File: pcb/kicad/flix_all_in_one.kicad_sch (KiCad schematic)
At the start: 0 parts

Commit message: Updated sch and added BoM.md
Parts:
- added U1: ESP32-WROOM-32E, RF_Module:ESP32-WROOM-32E, symbol RF_Module:ESP32-WROOM-32E
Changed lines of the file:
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@@
 	(generator_version "10.0")
 	(paper "A4")
+	(symbol
+		(lib_id "RF_Module:ESP32-WROOM-32E")
+		(at 148.59 102.87 0)
+		(unit 1)
+		(body_style 1)
+		(exclude_from_sim no)
+		(in_bom yes)
+		(on_board yes)
+		(in_pos_files yes)
+		(dnp no)
+		(fields_autoplaced yes)
+		(property "Reference" "U1"
+			(at 150.7333 64.77 0)
+			(show_name no)
+			(do_not_autoplace no)
+			(effects
+				(font
+					(size 1.27 1.27)
+				)
+				(justify left)
+			)
+		)
+		(property "Value" "ESP32-WROOM-32E"
+			(at 150.7333 67.31 0)
+			(show_name no)
+			(do_not_autoplace no)
+			(effects
+				(font
+					(size 1.27 1.27)
+				)
+				(justify left)
+			)
+		)
+		(property "Footprint" "RF_Module:ESP32-WROOM-32E"
+			(at 165.1 137.16 0)
+			(hide yes)
+			(show_name no)
+			(do_not_autoplace no)
+			(effects
+				(font
+					(size 1.27 1.27)
+				)
+			)
+		)
+		(property "Datasheet" "https://www.espressif.com/sites/default/files/documentation/esp32-wroom-32e_esp32-wroom-32ue_datasheet_en.pdf"
+			(at 148.59 102.87 0)
+			(hide yes)
+			(show_name no)
+			(do_not_autoplace no)
+			(effects
+				(font
+					(size 1.27 1.27)
+				)
+			)
+		)
+		(property "Description" "RF Module, ESP32-D0WD-V3 SoC, without PSRAM, Wi-Fi 802.11b/g/n, Bluetooth, BLE, 32-bit, 2.7-3.6V, onboard antenna, SMD"
+			(at 148.59 102.87 0)
+			(hide yes)
+			(show_name no)
+			(do_not_autoplace no)
+			(effects
+				(font
+					(size 1.27 1.27)
+				)
+			)
+		)
+		(pin "14"
+		)
+		(pin "11"
+		)
+		(pin "16"
+		)
+		(pin "12"
+		)
+		(pin "9"
+		)
+		(pin "17"
+		)
+		(pin "13"
+		)
+		(pin "30"
+		)
+		(pin "33"
+		)
+		(pin "27"
+		)
+		(pin "31"
+		)
+		(pin "10"
+		)
+		(pin "32"
+		)
+		(pin "34"
+		)
+		(pin "18"
+		)
+		(pin "26"
+		)
+		(pin "28"
+		)
+		(pin "19"
+		)
+		(pin "21"
+		)
+		(pin "35"
+		)
+		(pin "36"
+		)
+		(pin "29"
+		)
+		(pin "[1,15,38,39]"
+		)
+		(pin "3"
+		)
+		(pin "2"
+		)
+		(pin "20"
+		)
+		(pin "4"
+		)
+		(pin "25"
+		)
+		(pin "6"
+		)
+		(pin "24"
+		)
+		(pin "5"
+		)
+		(pin "7"
+		)
+		(pin "8"
+		)
+		(pin "37"
+		)
+		(pin "22"
+		)
+		(pin "23"
+		)
+		(instances
+			(project "flix_all_in_one"
+				(path "/b72e5080-03e0-4f53-a508-ed803e54cf11"
+					(reference "U1")
+					(unit 1)
+				)
+			)
+		)
+	)
 	(sheet_instances
 		(path "/"

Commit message: .
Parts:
- removed U1: ESP32-WROOM-32E, RF_Module:ESP32-WROOM-32E, symbol RF_Module:ESP32-WROOM-32E
- added U1: ESP32-WROOM-E, PCM_Espressif:ESP32-WROOM-32E, symbol PCM_Espressif:ESP32-WROOM-E
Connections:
- new net: U1.1 (GND), U1.15 (GND), U1.38 (GND)
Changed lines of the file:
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@@
 	(paper "A4")
 	(symbol
-		(lib_id "RF_Module:ESP32-WROOM-32E")
-		(at 148.59 102.87 0)
+		(lib_id "PCM_Espressif:ESP32-WROOM-E")
+		(at 195.58 68.58 0)
 		(unit 1)
 		(body_style 1)
@@
 		(fields_autoplaced yes)
 		(property "Reference" "U1"
-			(at 150.7333 64.77 0)
+			(at 197.7233 40.64 0)
 			(show_name no)
 			(do_not_autoplace no)
@@
 			)
 		)
-		(property "Value" "ESP32-WROOM-32E"
-			(at 150.7333 67.31 0)
+		(property "Value" "ESP32-WROOM-E"
+			(at 197.7233 43.18 0)
 			(show_name no)
 			(do_not_autoplace no)
@@
 			)
 		)
-		(property "Footprint" "RF_Module:ESP32-WROOM-32E"
-			(at 165.1 137.16 0)
+		(property "Footprint" "PCM_Espressif:ESP32-WROOM-32E"
+			(at 195.58 104.14 0)
 			(hide yes)
 			(show_name no)
@@
 		)
 		(property "Datasheet" "https://www.espressif.com/sites/default/files/documentation/esp32-wroom-32e_esp32-wroom-32ue_datasheet_en.pdf"
-			(at 148.59 102.87 0)
+			(at 195.58 106.68 0)
 			(hide yes)
 			(show_name no)
@@
 			)
 		)
-		(property "Description" "RF Module, ESP32-D0WD-V3 SoC, without PSRAM, Wi-Fi 802.11b/g/n, Bluetooth, BLE, 32-bit, 2.7-3.6V, onboard antenna, SMD"
-			(at 148.59 102.87 0)
+		(property "Description" "ESP32-WROOM-32E integrates ESP32-D0WD-V3, with higher stability and safety performance."
+			(at 195.58 68.58 0)
 			(hide yes)
 			(show_name no)
@@
 			)
 		)
-		(pin "14"
+		(pin "15"
 		)
-		(pin "11"
+		(pin "30"
 		)
-		(pin "16"
-		)
-		(pin "12"
-		)
-		(pin "9"
-		)
-		(pin "17"
+		(pin "31"
 		)
 		(pin "13"
 		)
-		(pin "30"
-		)
-		(pin "33"
-		)
-		(pin "27"
-		)
-		(pin "31"
-		)
-		(pin "10"
-		)
-		(pin "32"
-		)
-		(pin "34"
-		)
-		(pin "18"
-		)
-		(pin "26"
-		)
-		(pin "28"
-		)
-		(pin "19"
-		)
-		(pin "21"
+		(pin "25"
 		)
 		(pin "35"
@@
 		(pin "36"
 		)
+		(pin "33"
+		)
 		(pin "29"
 		)
-		(pin "[1,15,38,39]"
+		(pin "34"
+		)
+		(pin "37"
+		)
+		(pin "14"
+		)
+		(pin "7"
+		)
+		(pin "26"
+		)
+		(pin "9"
+		)
+		(pin "27"
+		)
+		(pin "5"
+		)
+		(pin "4"
 		)
 		(pin "3"
 		)
-		(pin "2"
+		(pin "23"
 		)
-		(pin "20"
+		(pin "39"
 		)
-		(pin "4"
+		(pin "12"
 		)
-		(pin "25"
+		(pin "28"
+		)
+		(pin "16"
+		)
+		(pin "38"
+		)
+		(pin "11"
+		)
+		(pin "8"
+		)
+		(pin "10"
 		)
 		(pin "6"
 		)
+		(pin "2"
+		)
+		(pin "1"
+		)
 		(pin "24"
 		)
-		(pin "5"
-		)
-		(pin "7"
-		)
-		(pin "8"
-		)
-		(pin "37"
-		)
-		(pin "22"
-		)
-		(pin "23"
-		)
 		(instances

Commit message: updated sch
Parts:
- added IC1: CP2102C-A01-GQFN28, QFN50P500X500X80-29N-D, symbol CP2102C-A01-GQFN28:CP2102C-A01-GQFN28
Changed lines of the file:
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@@
 	(paper "A4")
+	(symbol
+		(lib_id "CP2102C-A01-GQFN28:CP2102C-A01-GQFN28")
+		(at 45.72 48.26 0)
+		(unit 1)
+		(body_style 1)
+		(exclude_from_sim no)
+		(in_bom yes)
+		(on_board yes)
+		(in_pos_files yes)
+		(dnp no)
+		(fields_autoplaced yes)
+		(property "Reference" "IC1"
+			(at 86.36 41.8398 0)
+			(show_name no)
+			(do_not_autoplace no)
+			(effects
+				(font
+					(size 1.27 1.27)
+				)
+			)
+		)
+		(property "Value" "CP2102C-A01-GQFN28"
+			(at 86.36 44.3798 0)
+			(show_name no)
+			(do_not_autoplace no)
+			(effects
+				(font
+					(size 1.27 1.27)
+				)
+			)
+		)
+		(property "Footprint" "QFN50P500X500X80-29N-D"
+			(at 74.93 133.02 0)
+			(hide yes)
+			(show_name no)
+			(do_not_autoplace no)
+			(effects
+				(font
+					(size 1.27 1.27)
+				)
+				(justify left top)
+			)
+		)
+		(property "Datasheet" "https://www.silabs.com/documents/public/data-sheets/cp2102c-datasheet.pdf"
+			(at 74.93 233.02 0)
+			(hide yes)
+			(show_name no)
+			(do_not_autoplace no)
+			(effects
+				(font
+					(size 1.27 1.27)
+				)
+				(justify left top)
+			)
+		)
+		(property "Description" "USB Interface IC Single Chip - USB to UART Bridge QFN28 -40 to +85 C"
+			(at 45.72 48.26 0)
+			(hide yes)
+			(show_name no)
+			(do_not_autoplace no)
+			(effects
+				(font
+					(size 1.27 1.27)
+				)
+			)
+		)
+		(property "Height" "0.8"
+			(at 74.93 433.02 0)
+			(hide yes)
+			(show_name no)
+			(do_not_autoplace no)
+			(effects
+				(font
+					(size 1.27 1.27)
+				)
+				(justify left top)
+			)
+		)
+		(property "Mouser Part Number" "634-P2102CA01GQFN28"
+			(at 74.93 533.02 0)
+			(hide yes)
+			(show_name no)
+			(do_not_autoplace no)
+			(effects
+				(font
+					(size 1.27 1.27)
+				)
+				(justify left top)
+			)
+		)
+		(property "Mouser Price/Stock" "https://www.mouser.co.uk/ProductDetail/Silicon-Labs/CP2102C-A01-GQFN28?qs=NeOn4crkEus2KwttjYlKhg%3D%3D"
+			(at 74.93 633.02 0)
+			(hide yes)
+			(show_name no)
+			(do_not_autoplace no)
+			(effects
+				(font
+					(size 1.27 1.27)
+				)
+				(justify left top)
+			)
+		)
+		(property "Manufacturer_Name" "Silicon Labs"
+			(at 74.93 733.02 0)
+			(hide yes)
+			(show_name no)
+			(do_not_autoplace no)
+			(effects
+				(font
+					(size 1.27 1.27)
+				)
+				(justify left top)
+			)
+		)
+		(property "Manufacturer_Part_Number" "CP2102C-A01-GQFN28"
+			(at 74.93 833.02 0)
+			(hide yes)
+			(show_name no)
+			(do_not_autoplace no)
+			(effects
+				(font
+					(size 1.27 1.27)
+				)
+				(justify left top)
+			)
+		)
+		(pin "10"
+		)
+		(pin "12"
+		)
+		(pin "14"
+		)
+		(pin "13"
+		)
+		(pin "11"
+		)
+		(pin "15"
+		)
+		(pin "9"
+		)
+		(pin "3"
+		)
+		(pin "6"
+		)
+		(pin "7"
+		)
+		(pin "2"
+		)
+		(pin "5"
+		)
+		(pin "4"
+		)
+		(pin "19"
+		)
+		(pin "1"
+		)
+		(pin "17"
+		)
+		(pin "28"
+		)
+		(pin "20"
+		)
+		(pin "21"
+		)
+		(pin "18"
+		)
+		(pin "8"
+		)
+		(pin "29"
+		)
+		(pin "22"
+		)
+		(pin "23"
+		)
+		(pin "24"
+		)
+		(pin "16"
+		)
+		(pin "25"
+		)
+		(pin "26"
+		)
+		(pin "27"
+		)
+		(instances
+			(project "flix_all_in_one"
+				(path "/b72e5080-03e0-4f53-a508-ed803e54cf11"
+					(reference "IC1")
+					(unit 1)
+				)
+			)
+		)
+	)
 	(symbol
 		(lib_id "PCM_Espressif:ESP32-WROOM-E")

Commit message: updated BoM, Libs and SCH
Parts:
- added D1, D2, D3: SLESD5LM5.0CS, SODFL1608X70N, symbol SLESD5LM5.0CS:SLESD5LM5.0CS
- added IC2: BMP384, BMP384, symbol BMP384:BMP384
- added J1: UJ20-C-H-G-MSMT-2B-P16-TR, UJ20-C-H-G-MSMT-2B-P16-TR:SAMESKY_UJ20-C-H-G-MSMT-2B-P16-TR, symbol UJ20-C-H-G-MSMT-2B-P16-TR:UJ20-C-H-G-MSMT-2B-P16-TR
- added J2: BM03B-GHS-TBT_LF__SN__N_, BM03B-GHS-TBT_LF__SN__N_:CONN_BM03B-GHS-TBT_LF__SN__N_, symbol BM03B-GHS-TBT_LF__SN__N_:BM03B-GHS-TBT_LF__SN__N_
- added J3, J4, J5: BM02B-GHS-TBT_LF__SN__N_, BM02B-GHS-TBT_LF__SN__N_:JST_BM02B-GHS-TBT_LF__SN__N_, symbol BM02B-GHS-TBT_LF__SN__N_:BM02B-GHS-TBT_LF__SN__N_
- added S1: TS21-34-035-BK-260-SMT-TR, TS21-34-035-BK-260-SMT-TR:SW_TS21-34-035-BK-260-SMT-TR, symbol TS21-34-035-BK-260-SMT-TR:TS21-34-035-BK-260-SMT-TR
- added U2: ICM-40609-D, ICM-40609-D:XDCR_ICM-40609-D, symbol ICM-40609-D:ICM-40609-D
- added U3: TP4054ST25P, C382138:SOT-23-5_L2.9-W1.6-P0.95-LS2.8-BL, symbol TP4054ST25P:TP4054ST25P
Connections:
- new net: J1.SH1 (SHIELD), J1.SH2 (SHIELD), J1.SH3 (SHIELD), J1.SH4 (SHIELD)
- new net: U2.1 (NC), U2.10 (NC), U2.14 (NC), U2.15 (NC), U2.16 (NC), U2.17 (NC), U2.2 (NC), U2.21 (NC), U2.3 (NC), U2.4 (NC), U2.5 (NC), U2.6 (NC), U2.7 (NC)
- new net: U2.11 (RESV), U2.20 (RESV)
- new net: J5.S1 (SHIELD), J5.S2 (SHIELD)
- new net: J4.S1 (SHIELD), J4.S2 (SHIELD)
- new net: J3.S1 (SHIELD), J3.S2 (SHIELD)
- new net: J2.4 (SHIELD), J2.5 (SHIELD)
- new net GND: J1.A1/B12 (GND), J1.B1/A12 (GND)
- new net VBUS: J1.A4/B9 (VBUS), J1.B4/A9 (VBUS)

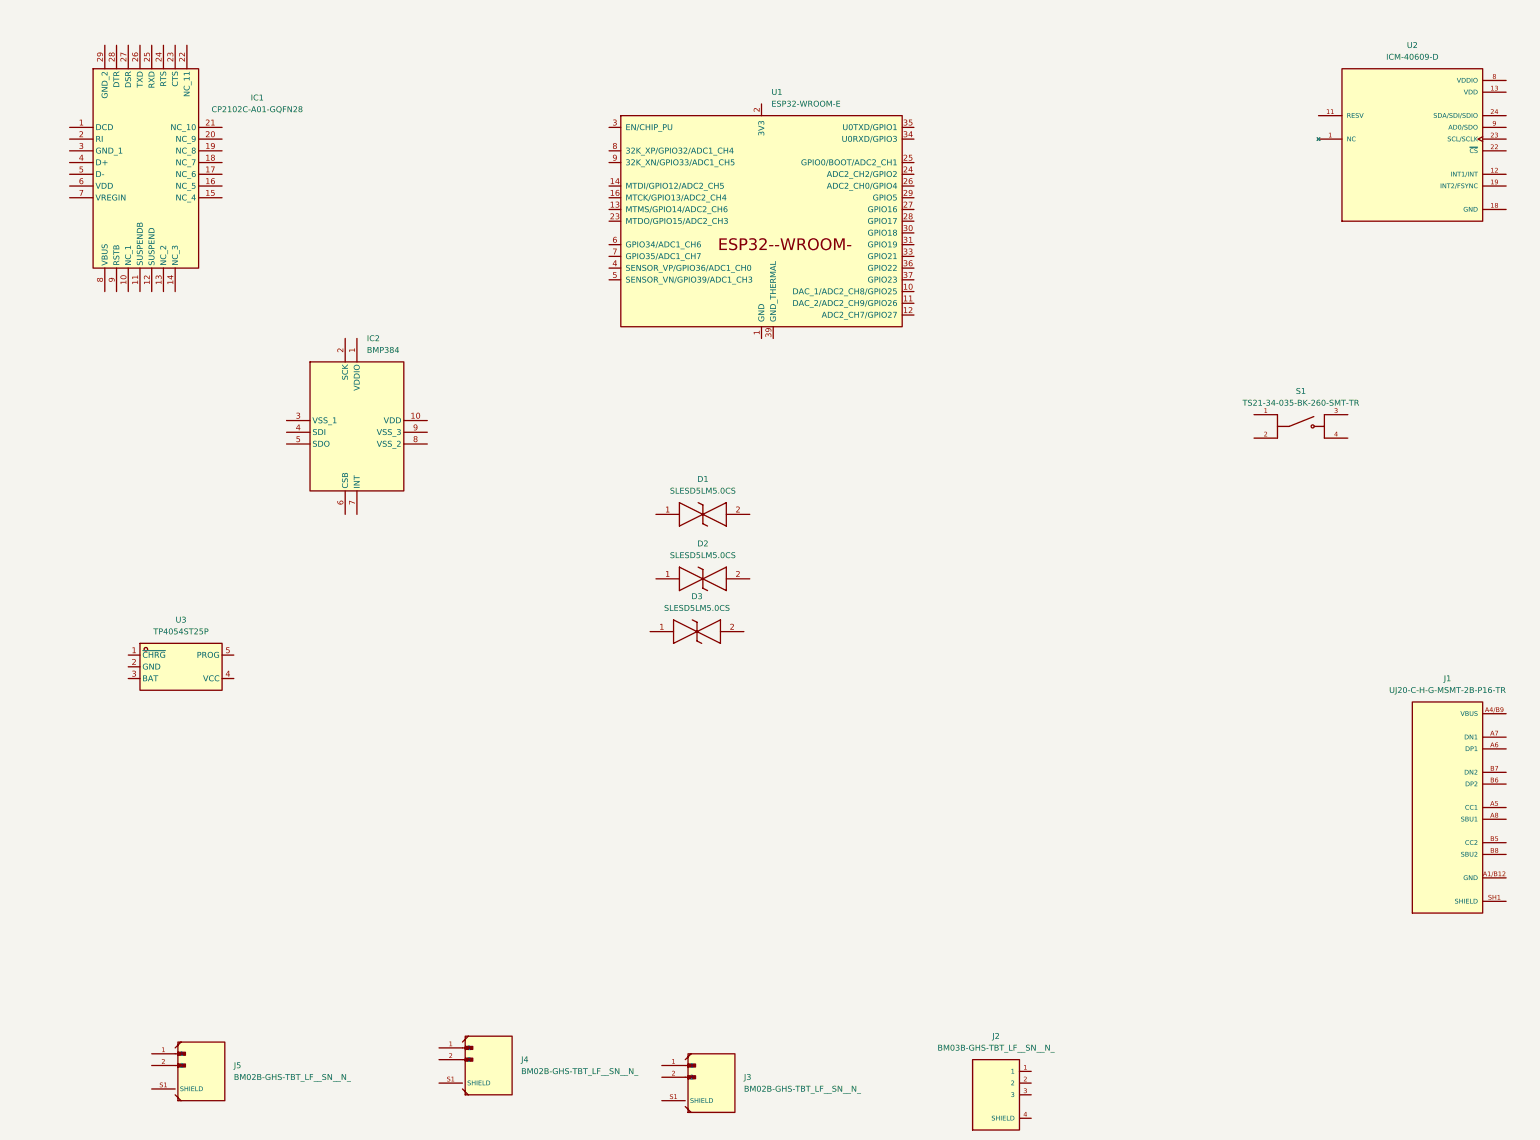
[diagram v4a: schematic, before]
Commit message: update lib and sch
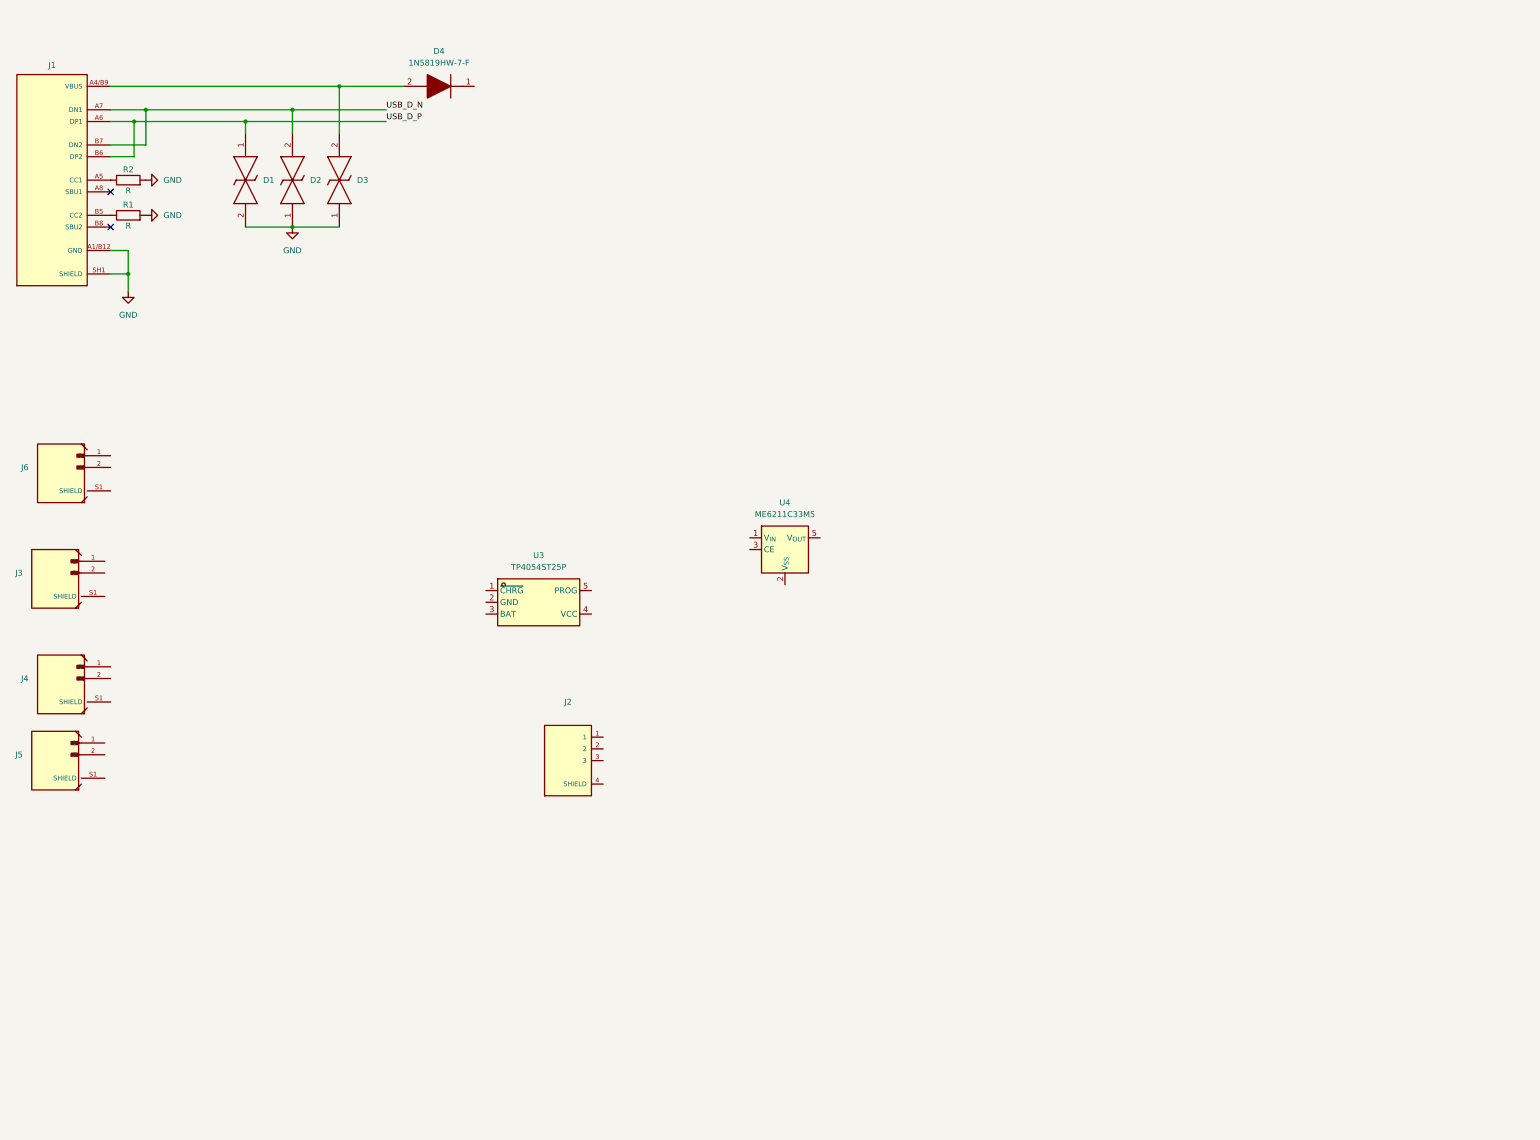
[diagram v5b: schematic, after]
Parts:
- removed IC1: CP2102C-A01-GQFN28, QFN50P500X500X80-29N-D, symbol CP2102C-A01-GQFN28:CP2102C-A01-GQFN28
- removed IC2: BMP384, BMP384, symbol BMP384:BMP384
- removed S1: TS21-34-035-BK-260-SMT-TR, TS21-34-035-BK-260-SMT-TR:SW_TS21-34-035-BK-260-SMT-TR, symbol TS21-34-035-BK-260-SMT-TR:TS21-34-035-BK-260-SMT-TR
- removed U1: ESP32-WROOM-E, PCM_Espressif:ESP32-WROOM-32E, symbol PCM_Espressif:ESP32-WROOM-E
- removed U2: ICM-40609-D, ICM-40609-D:XDCR_ICM-40609-D, symbol ICM-40609-D:ICM-40609-D
- added D4: 1N5819HW-7-F, SOD3716X125N, symbol 1N5819HW-7-F:1N5819HW-7-F
- added J6: BM02B-GHS-TBT_LF__SN__N_, BM02B-GHS-TBT_LF__SN__N_:JST_BM02B-GHS-TBT_LF__SN__N_, symbol BM02B-GHS-TBT_LF__SN__N_:BM02B-GHS-TBT_LF__SN__N_
- added R1, R2: R, symbol Device:R
- added U4: ME6211C33M5, Package_TO_SOT_SMD:SOT-23-5, symbol Regulator_Linear:ME6211C33M5
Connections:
- net GND: now also D1.2, D2.1, D3.1, J1.SH1 (SHIELD), J1.SH2 (SHIELD), J1.SH3 (SHIELD), J1.SH4 (SHIELD), R1.2, R2.2
- net VBUS: now also D3.2, D4.2 (A)
- net at J1.A5 (CC1): now also R2.1
- net USB_D_P: now reaches J1.A6 (DP1)
- net USB_D_P: now also D1.1, J1.B6 (DP2)
- net USB_D_N: now reaches J1.A7 (DN1)
- net USB_D_N: now also D2.2, J1.B7 (DN2)
- net at J1.B5 (CC2): now also R1.1
- new net: J6.S1 (SHIELD), J6.S2 (SHIELD)
- no-connect marks 0 -> 2
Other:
- moved on the sheet: D2, D3, J1, J2, J3, J4, J5, U3

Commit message: update libs and sch
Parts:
- added C1, C2: C, symbol Device:C
- added J7: Conn_01x02_Pin, symbol Connector:Conn_01x02_Pin
- added Q2: SLMT320V4CP, SOT95P280X110-3N, symbol SLMT320V4CP:SLMT320V4CP
- added R3, R4: 100k, symbol Device:R
- R1, R2: value R -> 5k1
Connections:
- net GND: now also J2.3, J2.4 (SHIELD), J2.5 (SHIELD), J3.2, J3.S1 (SHIELD), J3.S2 (SHIELD), J4.2, J4.S1 (SHIELD), J4.S2 (SHIELD), J5.2, J5.S1 (SHIELD), J5.S2 (SHIELD), J6.S1 (SHIELD), J6.S2 (SHIELD), C1.2, C2.2, J7.2 (Pin_2), R3.2
- net VBUS: now also Q2.1 (G), R3.1
- net Motor_4_P: now reaches J5.1
- net V_In: now reaches D4.1 (K)
- net V_In: now also U4.1 (V_{IN}), C1.1, Q2.2 (S), R4.2
- net Motor_3_P: now reaches J4.1
- net Motor_2_P: now reaches J3.1
- net 5V_In: now reaches J2.1
- net S_Bus: now reaches J2.2
- net Motor_1_P: now reaches J6.1
- net at U4.3 (CE): now also R4.1
- net 3V3: now reaches U4.5 (V_{OUT})
- net 3V3: now also C2.1
- new net V_Batt: J7.1 (Pin_1), Q2.3 (D)
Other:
- moved on the sheet: D1, D2, D3, D4, J1, J2, J3, J4, J5, J6, R1, R2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
